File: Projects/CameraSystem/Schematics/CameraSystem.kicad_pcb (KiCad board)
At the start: 2 copper layers, 100 x 100 mm, 111 parts, among them J1 10118192-0001LF, J10 Conn_02x02_Odd_Even, J11 Conn_01x06, J12 Conn_01x06, J13 Conn_02x02_Odd_Even, J14 Conn_02x05_Odd_Even, J2 Conn_02x03_Odd_Even, J3 Conn_01x02, J4 Conn_01x03, J5 Conn_01x02, J6 Conn_02x02_Odd_Even, J7 Conn_02x02_Odd_Even, J8 DM3D-SF, J9 Conn_02x02_Odd_Even, K1 TouchPad, K2 TouchPad, K3 TouchPad, K4 TouchPad, K5 TouchPad, K6 TouchPad, K7 TouchPad, Q1 BC846B_215, Q2 BC846B_215, Q3 BC846B_215, Q4 BC846B_215, U1 CH340, U10 AT42QT1070-SSUR, U2 AZ1117CD-3.3TRG1DICT-ND, U3 ATMEGA16A-AU, U4 ESP8266, U5 MC74HC125ADTR2G, U6 OV7670, U7 SIT2001BI-S2-33E-24.000000G, U8 PCA9306D_118, U9 LCD_2x16_w_i2c, Y1 ABLS-12.000MHZ-B2-T, Y2 ABLS2-10.000MHZ-D4Y-T

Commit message: feat: layout updated
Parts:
- added REF**: MountingHole_3.2mm_M3, MountingHole:MountingHole_3.2mm_M3, F.Cu at (117.0, 117.0)
- added REF**: MountingHole_3.2mm_M3, MountingHole:MountingHole_3.2mm_M3, F.Cu at (23.0, 117.0)
- added REF**: MountingHole_3.2mm_M3, MountingHole:MountingHole_3.2mm_M3, F.Cu at (23.0, 94.4)
- added REF**: MountingHole_3.2mm_M3, MountingHole:MountingHole_3.2mm_M3, F.Cu at (124.2, 25.9)
- moved U7 10.6 mm to (89.5, 43.2), turned to 0 degrees
- moved C22 7.49 mm to (86.1, 43.7)
- moved C26 2.30 mm to (113.5, 118.0), turned to 270 degrees
- moved U10 1.58 mm to (108.2, 113.4)
- moved J9 1.02 mm to (98.8, 43.7)
- moved Q2 1.02 mm to (98.6, 38.2)
- moved R26 1.02 mm to (102.1, 38.9)
- moved R27 1.02 mm to (94.3, 37.2)
- moved R28 1.02 mm to (94.3, 39.2)
- moved J10 0.91 mm to (98.9, 55.1)
- moved R38 0.74 mm to (98.3, 117.4)
- moved R39 0.74 mm to (98.3, 114.5)
- moved R40 0.74 mm to (98.4, 111.4)
- moved R41 0.74 mm to (101.4, 116.0)
- moved R43 0.74 mm to (101.3, 109.8)
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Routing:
- net /Camera/CAM_VSYNC: track 0.00 -> 49.5 mm, vias 0 -> 1
- net /Camera/CAM_PCLK: track 0.00 -> 45.9 mm, vias 0 -> 1
- net /Camera/VDD_3V3_IN: track 21.2 -> 65.5 mm
- net /Camera/CAM_HSYNC: track 0.00 -> 43.1 mm, vias 0 -> 1
- net /Camera/CAM_D1: track 0.00 -> 40.5 mm
- net /Camera/CAM_D0: track 0.00 -> 38.7 mm
- net /Camera/CAM_D3: track 0.00 -> 36.4 mm
- net /Camera/CAM_D2: track 0.00 -> 36.2 mm
- net /Camera/CAM_D7: track 0.00 -> 35.5 mm
- net /Camera/CAM_D5: track 0.00 -> 34.7 mm
- net /Camera/CAM_D6: track 0.00 -> 31.9 mm
- net /Camera/CAM_D4: track 0.00 -> 31.4 mm
- net /Camera/CAM_CLK: track 0.00 -> 26.4 mm, vias 0 -> 2
- net Net-(J10-Pad1): track 2.54 -> 15.5 mm
- net Net-(J10-Pad4): track 3.65 -> 14.7 mm, vias 0 -> 2
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
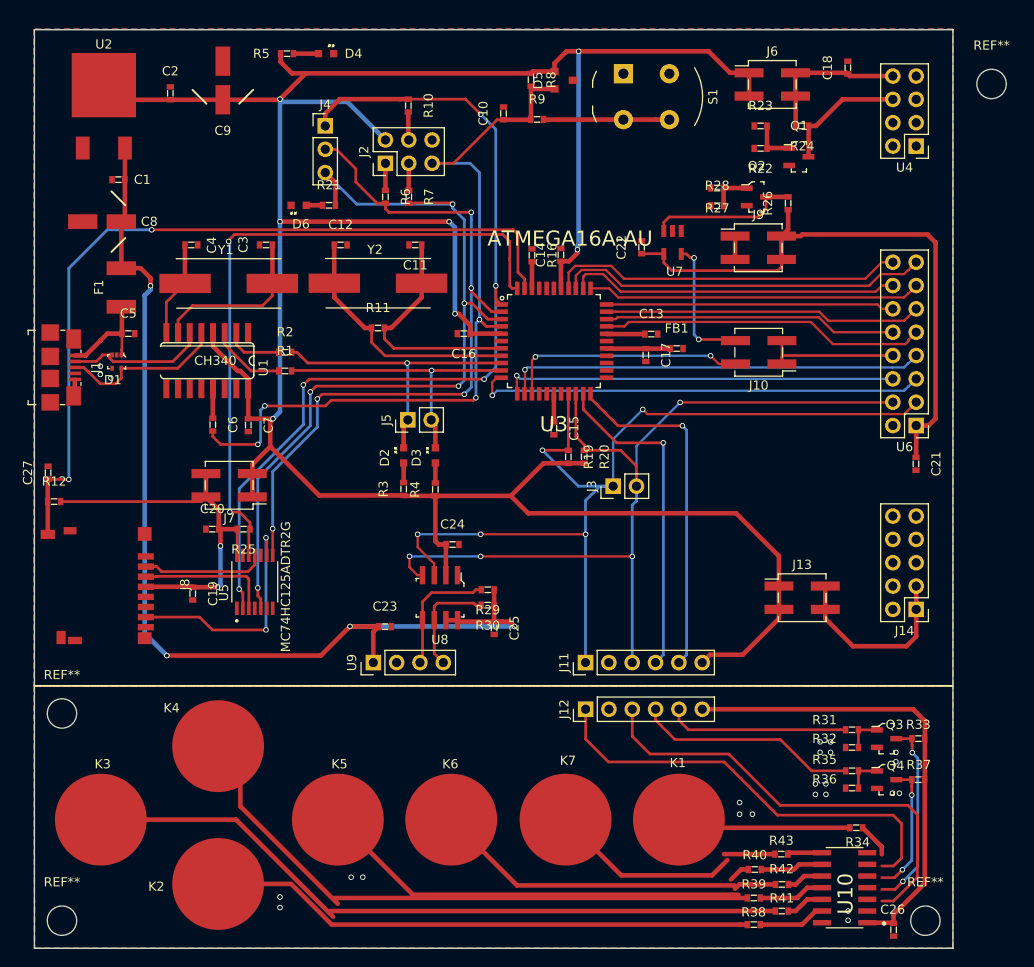
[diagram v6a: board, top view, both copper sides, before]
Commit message: feat: routing first draft finished
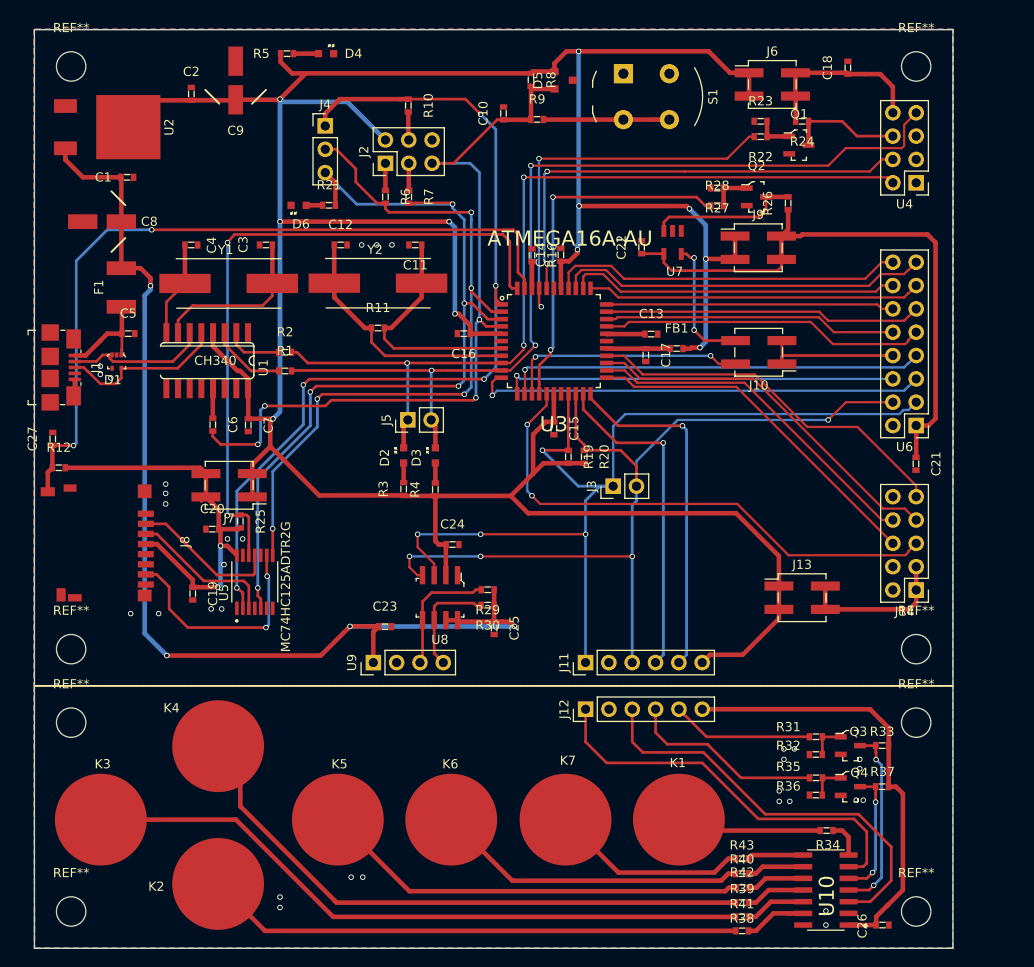
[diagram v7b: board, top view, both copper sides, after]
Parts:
- added REF**: MountingHole_3.2mm_M3, MountingHole:MountingHole_3.2mm_M3, F.Cu at (24.0, 24.0)
- added REF**: MountingHole_3.2mm_M3, MountingHole:MountingHole_3.2mm_M3, F.Cu at (24.0, 87.4)
- added REF**: MountingHole_3.2mm_M3, MountingHole:MountingHole_3.2mm_M3, F.Cu at (116.0, 87.4)
- added REF**: MountingHole_3.2mm_M3, MountingHole:MountingHole_3.2mm_M3, F.Cu at (116.0, 95.4)
- moved REF** 8.42 mm to (116.0, 24.0)
- moved U2 5.29 mm to (30.2, 30.6), turned to 270 degrees
- moved J8 4.65 mm to (32.1, 76.0)
- moved R41 4.39 mm to (97.0, 116.6)
- moved R43 4.32 mm to (97.0, 110.3)
- moved R42 4.30 mm to (97.1, 113.4)
- moved R33 4.01 mm to (112.3, 97.9)
- moved R35 4.01 mm to (105.1, 101.4)
- moved Q3 4.01 mm to (108.8, 97.9)
- moved Q4 4.01 mm to (108.8, 102.4)
- moved R31 4.01 mm to (105.1, 97.0)
- moved R32 4.01 mm to (105.1, 98.9)
- moved R36 4.01 mm to (105.1, 103.3)
- moved R37 4.01 mm to (112.3, 102.4)
- moved U4 4.00 mm to (116.0, 36.7)
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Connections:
- D1 pad 2: (no net) -> Net-(D1-Pad2)
- J1 pad 4: (no net) -> Net-(J1-Pad4)
- J14 pad 10: (no net) -> Net-(J14-Pad10)
- J14 pad 6: /Microcontroller/SENSOR1 -> /Microcontroller/M_DIR
- J14 pad 7: /Microcontroller/M_DIR -> /Microcontroller/SENSOR1
- J14 pad 8: /Microcontroller/SENSOR2 -> /Microcontroller/M_EN
- J14 pad 9: /Microcontroller/M_EN -> /Microcontroller/SENSOR2
- J8 pad 1: (no net) -> Net-(J8-Pad1)
- J8 pad 5: (no net) -> /Memory/SD_CLK_IN
- J8 pad 8: (no net) -> Net-(J8-Pad8)
- U1 pad 10: (no net) -> Net-(U1-Pad10)
- U1 pad 11: (no net) -> Net-(U1-Pad11)
- U1 pad 12: (no net) -> Net-(U1-Pad12)
- U1 pad 14: (no net) -> Net-(U1-Pad14)
- U1 pad 15: (no net) -> Net-(U1-Pad15)
- U1 pad 9: (no net) -> Net-(U1-Pad9)
- U4 pad 3: (no net) -> Net-(U4-Pad3)
- U4 pad 5: (no net) -> Net-(U4-Pad5)
- U5 pad 6: (no net) -> /Memory/SD_SCK_IN
- U7 pad 2: (no net) -> Net-(U7-Pad2)
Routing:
- net /Input_Interface/SPI_RX: track 31.5 -> 101.8 mm, vias 1 -> 3
- net /Microcontroller/SPI_RX: track 32.8 -> 95.0 mm, vias 1 -> 3
- net /Microcontroller/M_PWM: track 0.00 -> 57.3 mm, vias 0 -> 2
- net /Microcontroller/WIFI_EN: track 0.00 -> 51.2 mm, vias 0 -> 2
- net /Microcontroller/WIFI_RST: track 0.00 -> 42.8 mm, vias 0 -> 2
- net /Microcontroller/SENSOR1: track 0.00 -> 40.8 mm
- net /Microcontroller/SENSOR2: track 0.00 -> 40.8 mm
- net /Camera/CAM_XCLK_CTL: track 0.00 -> 39.6 mm, vias 0 -> 2
- net /Microcontroller/M_DIR: track 0.00 -> 38.6 mm
- net /Camera/VDD_3V3: track 317.9 -> 356.2 mm, vias 7 -> 11
- net /Microcontroller/M_EN: track 0.00 -> 37.9 mm
- net Net-(K7-Pad1): track 26.4 -> 21.5 mm
- net Net-(K5-Pad1): track 51.6 -> 46.7 mm
- net /Display/VDD_5V0: track 116.9 -> 121.6 mm
- net Net-(K3-Pad1): track 78.2 -> 73.5 mm
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
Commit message: feat: layout updated
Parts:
- removed REF** (x8): MountingHole_3.2mm_M3, MountingHole:MountingHole_3.2mm_M3
- D1: footprint digikey-footprints:SOT-553 -> custom-footprints:TPD2E001DRLR_no_stencil
- moved C21 1.59 mm to (115.4, 65.8), turned to 180 degrees
- moved C17 1.11 mm to (87.7, 55.4)
- moved D1 0.14 mm to (29.0, 56.3), turned to 270 degrees
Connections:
- D1 pad 2: Net-(D1-Pad2) -> /Input_Interface/USB_DN
- D1 pad 3: /Input_Interface/USB_DN -> /Input_Interface/USB_DP
- D1 pad 5: /Input_Interface/USB_DP -> /Input_Interface/USB_DN
- J1 pad 4: Net-(J1-Pad4) -> (no net)
- J14 pad 10: Net-(J14-Pad10) -> (no net)
- J8 pad 1: Net-(J8-Pad1) -> (no net)
- J8 pad 5: /Memory/SD_CLK_IN -> (no net)
- J8 pad 8: Net-(J8-Pad8) -> (no net)
- U1 pad 10: Net-(U1-Pad10) -> (no net)
- U1 pad 11: Net-(U1-Pad11) -> (no net)
- U1 pad 12: Net-(U1-Pad12) -> (no net)
- U1 pad 14: Net-(U1-Pad14) -> (no net)
- U1 pad 15: Net-(U1-Pad15) -> (no net)
- U1 pad 9: Net-(U1-Pad9) -> (no net)
- U4 pad 3: Net-(U4-Pad3) -> (no net)
- U4 pad 5: Net-(U4-Pad5) -> (no net)
- U5 pad 6: /Memory/SD_SCK_IN -> (no net)
- U7 pad 2: Net-(U7-Pad2) -> (no net)
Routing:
- net /Motor/VDD_3V3_CON_IN: track 16.6 -> 18.4 mm
- net /Camera/VDD_3V3_IN: track 65.5 -> 66.8 mm
- net /Input_Interface/USB_DP: track 18.2 -> 19.5 mm
- net /Input_Interface/USB_DN: track 15.6 -> 14.7 mm
- net GND: vias 16 -> 46
